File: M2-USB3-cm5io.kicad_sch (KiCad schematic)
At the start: 52 parts, among them J1 Bus_M.2_Socket_M, J2 Conn_01x16_MountingPin, J3 Conn_01x16_MountingPin, J4 USB3_A, U1 VL805, U18 MP3422GG-P, U2 W25Q32JVZP, U4 TLV62568ADRLR, Y1 25Mhz

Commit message: Fix most ERC/DRC errors
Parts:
- added R10: 10K, Resistor_SMD:R_0402_1005Metric, symbol Device:R
- J1: footprint NGFF:NGFF_M -> footprints:NGFF_M
- U18: symbol mp3422:MP3422GG-P -> symbols:MP3422GG-P
- U2: symbol Memory_Flash:W25Q32JVZP -> symbols:W25Q32JVZP
- U4: symbol 2021-10-17_21-20-06:TLV62568ADRLR -> symbols:TLV62568ADRLR
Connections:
- net +3.3VA: now also R10.1; no longer U2.7 (IO3)
- net USB3_RX1+: now also J2.10 (Pin_10), J3.7 (Pin_7); no longer J2.11 (Pin_11), J3.6 (Pin_6)
- net USB3_RX1-: now also J2.11 (Pin_11), J3.6 (Pin_6); no longer J2.10 (Pin_10), J3.7 (Pin_7)
- net PCIe_LED: no longer names the net of J1.10 (DAS/~{DSS}/~{LED1})
- new net: R10.2, U2.7 (IO3)
- no-connect marks 0 -> 39
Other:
- note added: "FFC on main board"
- note added: "USB Connector board"
- note removed: "TODO: - choose FFC connector - choose USB-A connector - choose 5v boost (steal from pipad probably?) - swap out SPI flash for W25Q10EW"
- moved on the sheet: C12

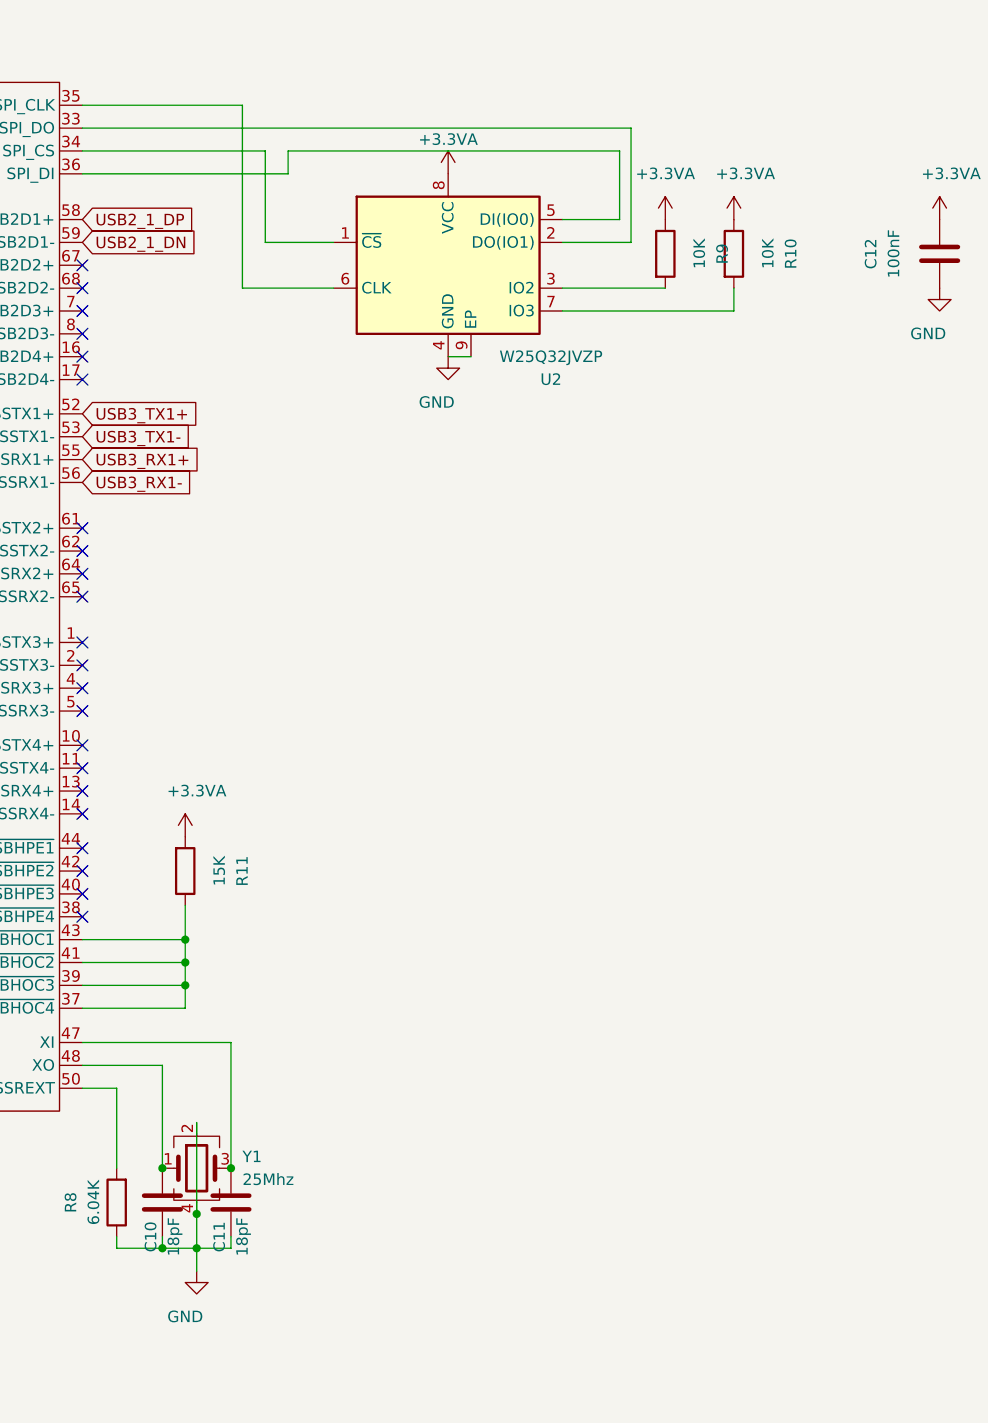
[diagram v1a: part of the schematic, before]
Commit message: Change some components to things I already have in stock
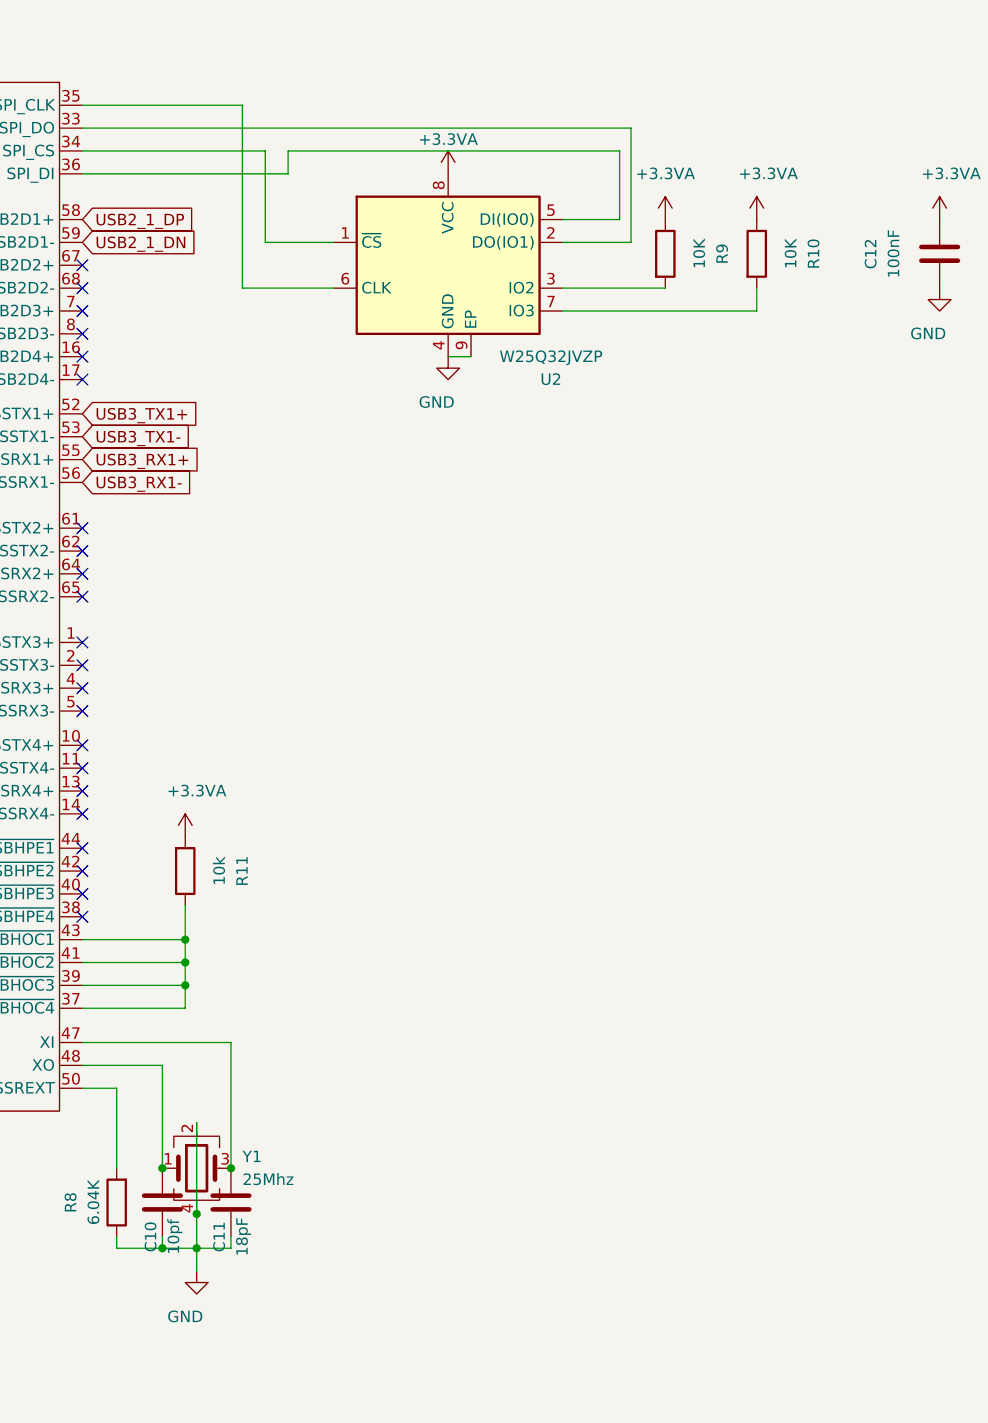
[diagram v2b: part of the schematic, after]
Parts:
- C10: value 18pF -> 10pf
- C4: footprint Capacitor_SMD:C_0603_1608Metric -> Capacitor_SMD:C_0805_2012Metric
- L1: footprint Inductor_SMD:L_Vishay_IHLP-1212 -> Inductor_SMD:L_1008_2520Metric
- R11: value 15K -> 10k
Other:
- moved on the sheet: R10
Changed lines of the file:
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@@
 	(wire
 		(pts
-			(xy 320.04 116.84) (xy 339.09 116.84)
+			(xy 320.04 116.84) (xy 341.63 116.84)
 		)
 		(stroke
@@
 	(wire
 		(pts
-			(xy 339.09 114.3) (xy 339.09 116.84)
+			(xy 341.63 114.3) (xy 341.63 116.84)
 		)
 		(stroke
@@
 			)
 		)
-		(property "Value" "18pF"
+		(property "Value" "10pf"
 			(at 276.86 219.71 90)
 			(effects
@@
 			)
 		)
-		(property "Footprint" "Inductor_SMD:L_Vishay_IHLP-1212"
+		(property "Footprint" "Inductor_SMD:L_1008_2520Metric"
 			(at 170.18 279.4 0)
 			(effects
@@
 			)
 		)
-		(property "Footprint" "Capacitor_SMD:C_0603_1608Metric"
+		(property "Footprint" "Capacitor_SMD:C_0805_2012Metric"
 			(at 122.2248 279.4 0)
 			(effects
@@
 			)
 		)
-		(property "Value" "15K"
+		(property "Value" "10k"
 			(at 281.94 179.07 90)
 			(effects
@@
 	(symbol
 		(lib_id "Device:R")
-		(at 339.09 110.49 0)
+		(at 341.63 110.49 0)
 		(unit 1)
 		(exclude_from_sim no)
@@
 		(dnp no)
 		(property "Reference" "R10"
-			(at 345.44 110.49 90)
+			(at 347.98 110.49 90)
 			(effects
 				(font
@@
 		)
 		(property "Value" "10K"
-			(at 342.9 110.49 90)
+			(at 345.44 110.49 90)
 			(effects
 				(font
@@
 		)
 		(property "Footprint" "Resistor_SMD:R_0402_1005Metric"
-			(at 337.312 110.49 90)
+			(at 339.852 110.49 90)
 			(effects
 				(font
@@
 		)
 		(property "Datasheet" "~"
-			(at 339.09 110.49 0)
+			(at 341.63 110.49 0)
 			(effects
 				(font
@@
 		)
 		(property "Description" ""
-			(at 339.09 110.49 0)
+			(at 341.63 110.49 0)
 			(effects
 				(font
@@
 	(symbol
 		(lib_id "power:+3.3VA")
-		(at 339.09 106.68 0)
+		(at 341.63 106.68 0)
 		(unit 1)
 		(exclude_from_sim no)
@@
 		(dnp no)
 		(property "Reference" "#PWR0105"
-			(at 339.09 110.49 0)
+			(at 341.63 110.49 0)
 			(effects
 				(font
@@
 		)
 		(property "Value" "+3.3VA"
-			(at 340.36 101.6 0)
+			(at 342.9 101.6 0)
 			(effects
 				(font
@@
 		)
 		(property "Footprint" ""
-			(at 339.09 106.68 0)
+			(at 341.63 106.68 0)
 			(effects
 				(font
@@
 		)
 		(property "Datasheet" ""
-			(at 339.09 106.68 0)
+			(at 341.63 106.68 0)
 			(effects
 				(font
@@
 		)
 		(property "Description" ""
-			(at 339.09 106.68 0)
+			(at 341.63 106.68 0)
 			(effects
 				(font
